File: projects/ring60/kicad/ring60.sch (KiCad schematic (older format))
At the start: 12 parts, among them IC1 ATMEGA328-P, K1 CONN_3, U1 DS1307, U2 TSOP39338, X1 20 MHz, X2 32,768 kHz

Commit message: layout of board
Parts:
- removed X1: 20 MHz, symbol CRYSTAL
- added J1: USB, symbol USB
- added R3, R4: 68, symbol R
- added R5: 1k5, symbol R
- added X1: CRYSTAL_RESONATOR, symbol CRYSTAL_RESONATOR
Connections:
- net GND: now also J1.4 (GND), X1.3 (GND)
- net VCC: now also J1.1 (Vbus), R5.1
- net RTC_X1: now reaches U1.1 (X1), X2.1
- net RTC_X2: now reaches U1.2 (X2), X2.2
- net VBAT: now reaches BT1.1 (+), U1.3 (VBAT)
- net SDA: now reaches IC1.27 ((PCINT12/SDA/ADC4)PC4), R1.2, U1.5 (SDA)
- net SCL: now reaches IC1.28 ((PCINT14/SCL/ADC5)PC5), R2.2, U1.6 (SCL)
- net IROUT: now reaches IC1.5 ((PCINT19/OC2B/INT1)PD3)
- net IROUT: now also U2.1 (OUT); no longer U1.7 (SQW/OUT)
- net AVR_X2: now reaches C3.2, IC1.10 ((PCINT7/XTAL2/TOSC2)PB7)
- net AVR_X2: now also X1.2 (XTAL2)
- net D-R: now reaches IC1.13 ((PCINT23/AIN1)PD7)
- net D-R: now also R4.1
- net LED_OUT: now reaches IC1.14 ((PCINT0/CLKO/ICP1)PB0), K1.1 (P1)
- net SQW: now reaches IC1.23 ((PCINT8/ADC0)PC0)
- net SQW: now also U1.7 (SQW/OUT)
- net D+R: now reaches IC1.4 ((PCINT18/INT0)PD2)
- net D+R: now also R3.1; no longer U2.1 (OUT)
- net AVR_X1: now reaches C2.2, IC1.9 ((PCINT6/XTAL1/TOSC1)PB6)
- net AVR_X1: now also X1.1 (XTAL1)
- new net D+: J1.3 (D+), R3.2
- new net D-: J1.2 (D-), R4.2, R5.2
- no-connect marks 14 -> 12
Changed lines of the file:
@@
 LIBS:valves
 LIBS:ring60
+LIBS:custom
+LIBS:ring60-cache
 EELAYER 24 0
 EELAYER END
@@
 $EndComp
 $Comp
-L CRYSTAL X1
-U 1 1 537ACF20
-P 7100 2200
-F 0 "X1" H 7100 2350 60  0000 C CNN
-F 1 "20 MHz" H 7100 2050 60  0000 C CNN
-F 2 "" H 7100 2200 60  0000 C CNN
-F 3 "" H 7100 2200 60  0000 C CNN
-	1    7100 2200
-	0    -1   -1   0
-$EndComp
-$Comp
 L CRYSTAL X2
 U 1 1 537ACF32
@@
 	6800 2400 6500 2400
 Wire Wire Line
-	6500 3700 10050 3700
-Wire Wire Line
-	10050 3700 10050 2000
-Wire Wire Line
-	10050 2000 9750 2000
+	9750 2000 10100 2000
 Wire Wire Line
 	6500 3150 9950 3150
@@
 Wire Wire Line
 	8900 4600 8900 4700
-Wire Wire Line
-	8900 4700 7900 4700
-Wire Wire Line
-	7900 4700 7900 3600
-Wire Wire Line
-	7900 3600 6500 3600
 $Comp
 L GND #PWR08
@@
 	4300 2400 4600 2400
 Connection ~ 4300 2100
-NoConn ~ 6500 2650
 NoConn ~ 6500 2750
 NoConn ~ 6500 2850
@@
 NoConn ~ 6500 3900
 NoConn ~ 6500 4000
-NoConn ~ 6500 4100
 NoConn ~ 6500 1900
 NoConn ~ 6500 2000
@@
 Wire Wire Line
 	8150 2000 8550 2000
+$Comp
+L USB J1
+U 1 1 537B5881
+P 7250 4950
+F 0 "J1" H 7200 5350 60  0000 C CNN
+F 1 "USB" V 7000 5100 60  0000 C CNN
+F 2 "" H 7250 4950 60  0000 C CNN
+F 3 "" H 7250 4950 60  0000 C CNN
+	1    7250 4950
+	1    0    0    -1
+$EndComp
+$Comp
+L GND #PWR013
+U 1 1 537B58A7
+P 6750 5300
+F 0 "#PWR013" H 6750 5300 30  0001 C CNN
+F 1 "GND" H 6750 5230 30  0001 C CNN
+F 2 "" H 6750 5300 60  0000 C CNN
+F 3 "" H 6750 5300 60  0000 C CNN
+	1    6750 5300
+	0    1    1    0
+$EndComp
+$Comp
+L VCC #PWR014
+U 1 1 537B58BD
+P 6750 5150
+F 0 "#PWR014" H 6750 5250 30  0001 C CNN
+F 1 "VCC" H 6750 5250 30  0000 C CNN
+F 2 "" H 6750 5150 60  0000 C CNN
+F 3 "" H 6750 5150 60  0000 C CNN
+	1    6750 5150
+	0    -1   -1   0
+$EndComp
+Wire Wire Line
+	6750 5150 6850 5150
+Wire Wire Line
+	6750 5300 6850 5300
+Wire Wire Line
+	6800 2650 6800 3500
+Wire Wire Line
+	6800 3500 10100 3500
+Wire Wire Line
+	10100 3500 10100 2000
+Wire Wire Line
+	6500 2650 6800 2650
+Wire Wire Line
+	6500 3700 8150 3700
+Wire Wire Line
+	7600 3600 6500 3600
+$Comp
+L R R3
+U 1 1 537B76C3
+P 7600 4650
+F 0 "R3" V 7680 4650 40  0000 C CNN
+F 1 "68" V 7607 4651 40  0000 C CNN
+F 2 "" V 7530 4650 30  0000 C CNN
+F 3 "" H 7600 4650 30  0000 C CNN
+	1    7600 4650
+	1    0    0    -1
+$EndComp
+$Comp
+L R R4
+U 1 1 537B76D5
+P 7800 4650
+F 0 "R4" V 7880 4650 40  0000 C CNN
+F 1 "68" V 7807 4651 40  0000 C CNN
+F 2 "" V 7730 4650 30  0000 C CNN
+F 3 "" H 7800 4650 30  0000 C CNN
+	1    7800 4650
+	1    0    0    -1
+$EndComp
+Wire Wire Line
+	7600 4900 7600 5150
+Wire Wire Line
+	7800 4900 7800 5300
+Wire Wire Line
+	7600 5300 7950 5300
+Wire Wire Line
+	7600 4400 7600 3600
+Wire Wire Line
+	6500 4100 7800 4100
+Wire Wire Line
+	7800 4100 7800 4400
+$Comp
+L R R5
+U 1 1 537B7813
+P 8200 5300
+F 0 "R5" V 8280 5300 40  0000 C CNN
+F 1 "1k5" V 8207 5301 40  0000 C CNN
+F 2 "" V 8130 5300 30  0000 C CNN
+F 3 "" H 8200 5300 30  0000 C CNN
+	1    8200 5300
+	0    1    1    0
+$EndComp
+Connection ~ 7800 5300
+$Comp
+L VCC #PWR015
+U 1 1 537B786E
+P 8550 5300
+F 0 "#PWR015" H 8550 5400 30  0001 C CNN
+F 1 "VCC" H 8550 5400 30  0000 C CNN
+F 2 "" H 8550 5300 60  0000 C CNN
+F 3 "" H 8550 5300 60  0000 C CNN
+	1    8550 5300
+	0    1    1    0
+$EndComp
+Wire Wire Line
+	8450 5300 8550 5300
+Wire Wire Line
+	8150 3700 8150 4700
+Wire Wire Line
+	8150 4700 8900 4700
+Text Label 8850 3500 0    60   ~ 0
+SQW
+Text Label 8850 3050 0    60   ~ 0
+SDA
+Text Label 8850 3150 0    60   ~ 0
+SCL
+Text Label 8400 4700 0    60   ~ 0
+IROUT
+Text Label 7600 4350 1    60   ~ 0
+D+R
+Text Label 7800 4350 1    60   ~ 0
+D-R
+Text Label 7600 5100 1    60   ~ 0
+D+
+Text Label 7800 5100 1    60   ~ 0
+D-
+Text Label 7000 2500 2    60   ~ 0
+AVR_X2
+Text Label 6800 2300 1    60   ~ 0
+AVR_X1
+Text Label 8200 1400 0    60   ~ 0
+RTC_X1
+Text Label 8200 2000 0    60   ~ 0
+RTC_X2
+Text Label 8200 2200 0    60   ~ 0
+VBAT
+Text Label 6700 1700 1    60   ~ 0
+LED_OUT
+$Comp
+L CRYSTAL_RESONATOR X1
+U 1 1 537BC555
+P 7100 2200
+F 0 "X1" H 7100 1950 60  0000 C CNN
+F 1 "CRYSTAL_RESONATOR" H 7100 2400 60  0000 C CNN
+F 2 "" H 7100 2200 60  0000 C CNN
+F 3 "" H 7100 2200 60  0000 C CNN
+	1    7100 2200
+	0    -1   1    0
+$EndComp
+Wire Wire Line
+	7100 2000 7100 1900
+Wire Wire Line
+	7100 2400 7100 2500
+Wire Wire Line
+	7250 2200 7600 2200
+Connection ~ 7600 2200
 $EndSCHEMATC

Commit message: working on ground plane
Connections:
- net GND: now also J1.5 (Shield_1), J1.6 (Shield_2)
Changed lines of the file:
@@
 	7250 2200 7600 2200
 Connection ~ 7600 2200
+Wire Wire Line
+	6850 5300 6850 5500
+Wire Wire Line
+	6850 5500 7600 5500
+Wire Wire Line
+	7600 5500 7600 5400
+Connection ~ 6850 5400
 $EndSCHEMATC

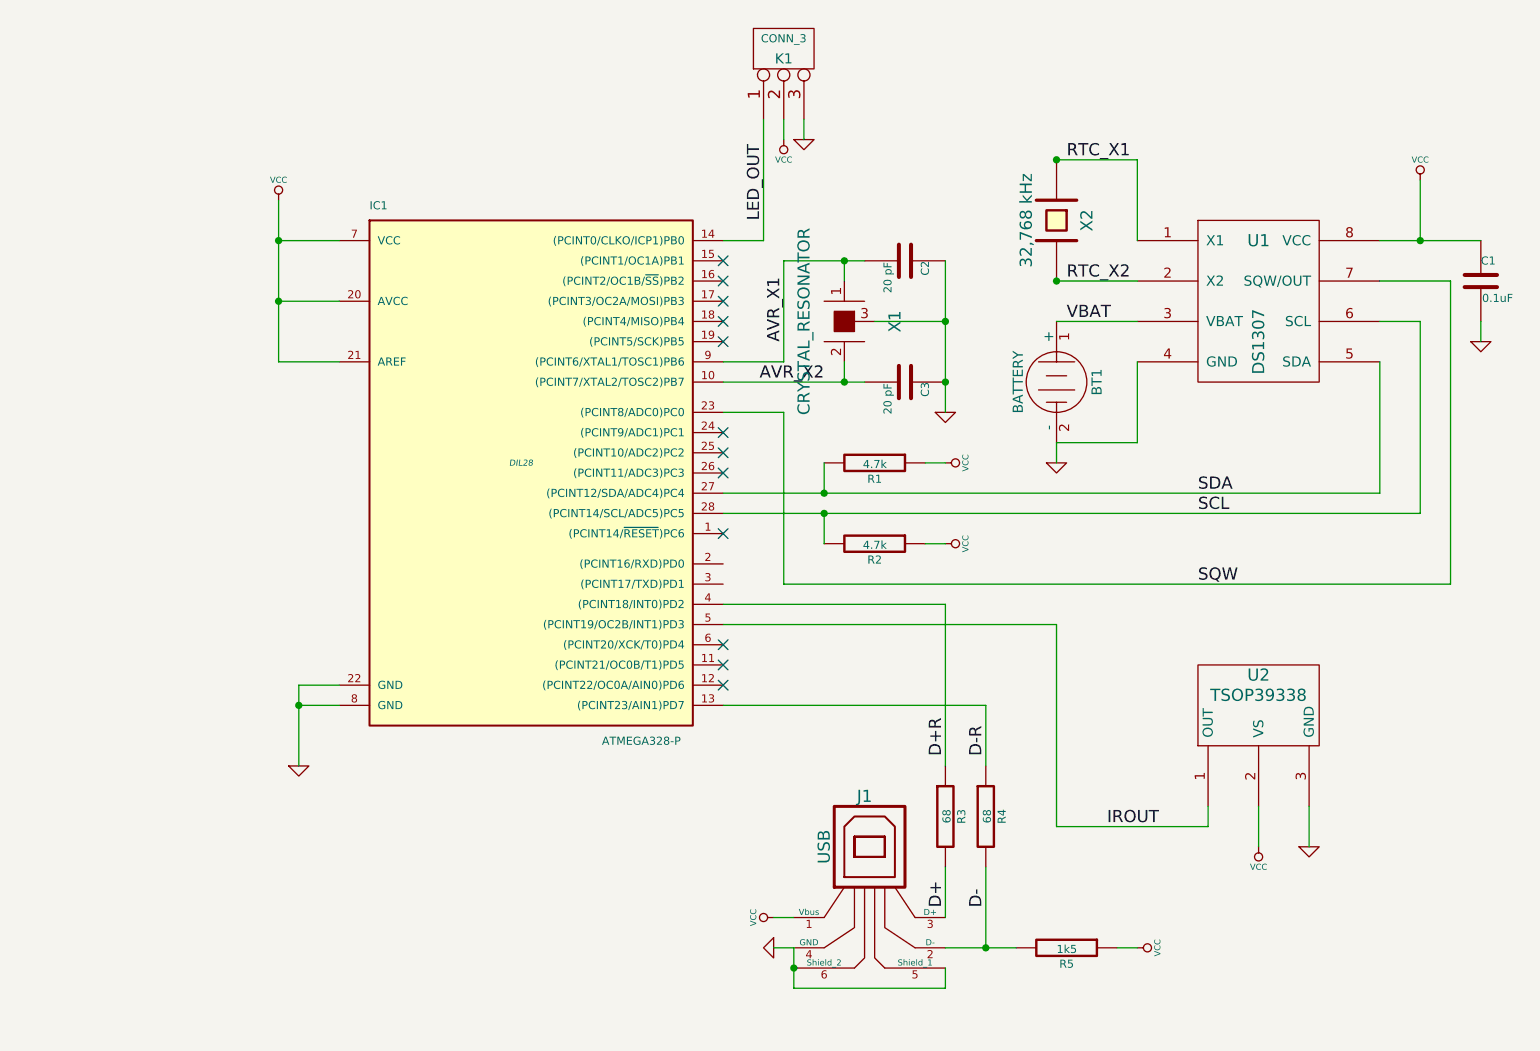
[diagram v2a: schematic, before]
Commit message: removed usb and made board smaller
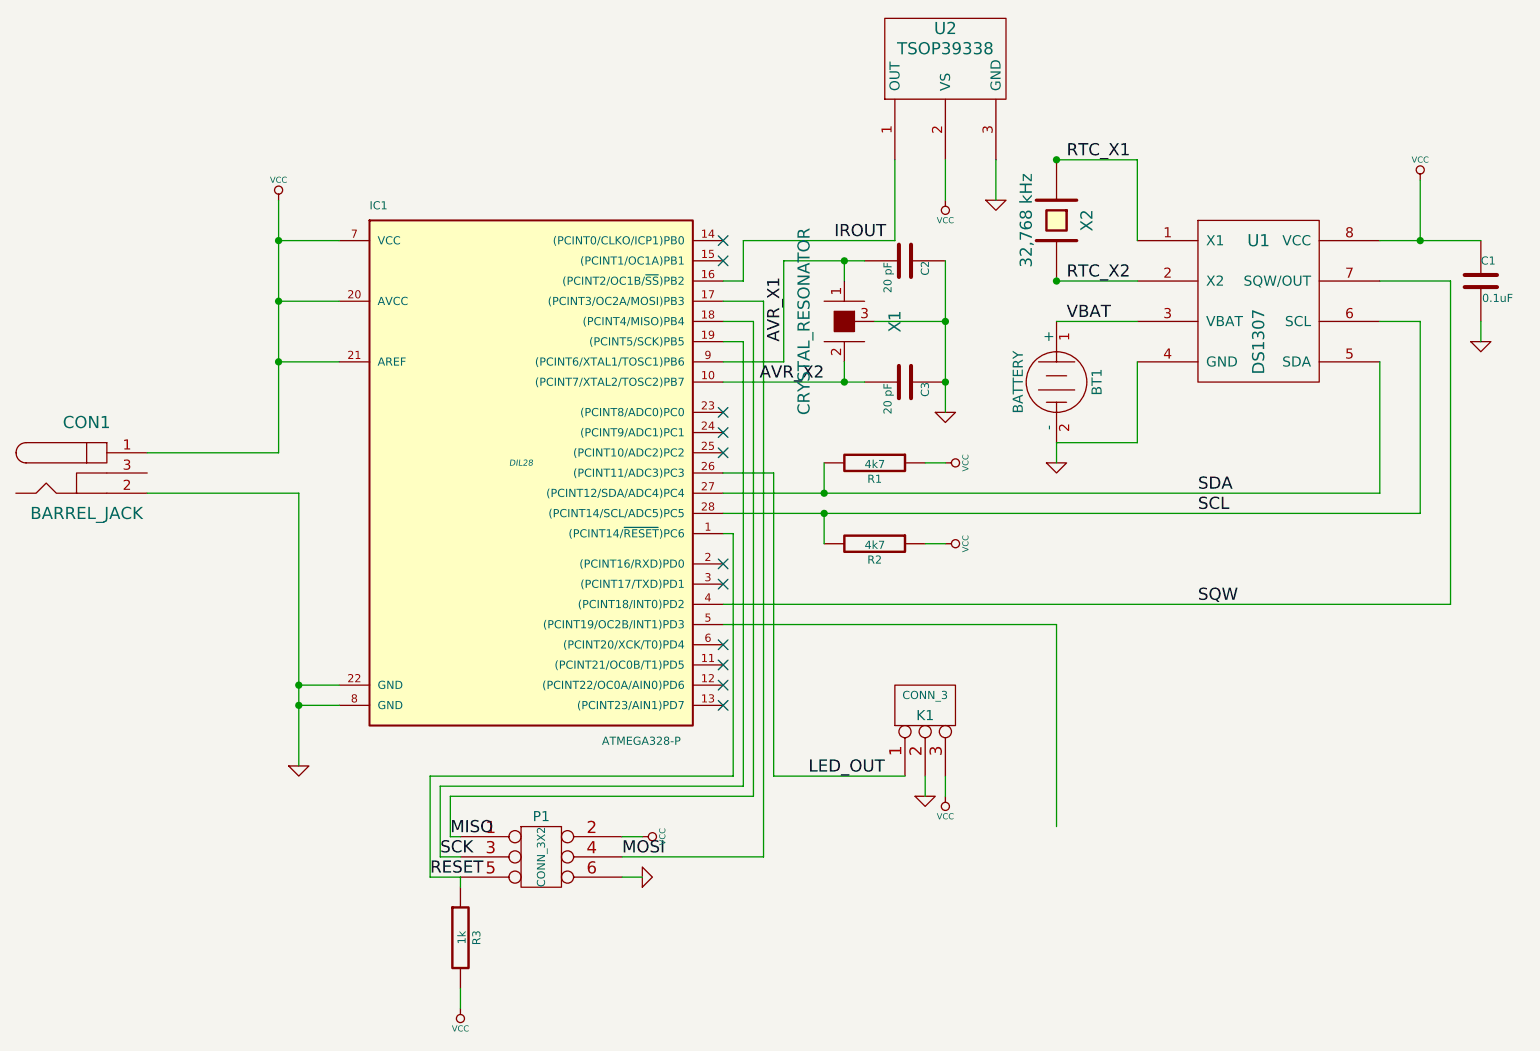
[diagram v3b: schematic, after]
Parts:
- removed J1: USB, symbol USB
- removed R4: 68, symbol R
- removed R5: 1k5, symbol R
- added CON1: BARREL_JACK, symbol BARREL_JACK
- added P1: CONN_3X2, symbol CONN_3X2
- R1, R2: value 4.7k -> 4k7
- R3: value 68 -> 1k
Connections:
- net D+ is gone; now on net VCC: R3.2
- net GND: now also K1.2 (PM), CON1.2, P1.6; no longer K1.3 (P3)
- net IROUT: now also IC1.16 ((PCINT2/OC1B/~SS~)PB2); no longer IC1.5 ((PCINT19/OC2B/INT1)PD3)
- net LED_OUT: now also IC1.26 ((PCINT11/ADC3)PC3); no longer IC1.14 ((PCINT0/CLKO/ICP1)PB0)
- net SQW: now also IC1.4 ((PCINT18/INT0)PD2); no longer IC1.23 ((PCINT8/ADC0)PC0)
- net VCC: now also K1.3 (P3), CON1.1, P1.2; no longer K1.2 (PM)
- net RESET: now reaches IC1.1 ((PCINT14/~RESET~)PC6)
- net RESET: now also R3.1, P1.5
- net MOSI: now reaches IC1.17 ((PCINT3/OC2A/MOSI)PB3)
- net MOSI: now also P1.4
- net MISO: now reaches IC1.18 ((PCINT4/MISO)PB4)
- net MISO: now also P1.1
- net SCK: now reaches IC1.19 ((PCINT5/SCK)PB5)
- net SCK: now also P1.3
- removed net D+R: IC1.4 ((PCINT18/INT0)PD2), R3.1
- net D-R: no longer names the net of IC1.13 ((PCINT23/AIN1)PD7)
- no-connect marks 12 -> 11
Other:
- moved on the sheet: K1, U2
